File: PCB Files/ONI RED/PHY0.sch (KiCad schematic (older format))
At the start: 40 parts

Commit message: Continued routing work
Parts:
- removed C? (x2): 22pF, symbol Device:C
- removed C? (x4): 0.1uF, symbol Device:C_Small
- removed R?: 12.1k, symbol Device:R
- removed R?: 4.7K, symbol Device:R
- removed R?: 220, symbol Device:R_Small
- removed R?: 1k, symbol Device:R_Small
- removed R?: 4.7k, symbol Device:R_Small
- removed U?: KSZ9031RNXCA, Package_DFN_QFN:QFN-48-1EP_7x7mm_P0.5mm_EP5.15x5.15mm, symbol Interface_Ethernet:KSZ9031RNXCA
- removed Y?: 25MHz, symbol Device:Crystal
- added C23, C24: 22pF, symbol Device:C
- added C25, C26, C27, C28: 0.1uF, symbol Device:C_Small
- added R13: 4.7K, symbol Device:R
- added R15: 12.1k, symbol Device:R
- added R18: 1k, symbol Device:R_Small
- added R19: 220, symbol Device:R_Small
- added R7: 4.7k, symbol Device:R_Small
- added U4: KSZ9031RNXCA, Package_DFN_QFN:QFN-48-1EP_7x7mm_P0.5mm_EP5.15x5.15mm, symbol Interface_Ethernet:KSZ9031RNXCA
- added Y1: 25MHz, symbol Device:Crystal
- C10, C16: renamed from C?; value 0.1uF -> 100nF
- C11, C14, C17, C22: renamed from C?; value 0.1uF -> 10uF
- C12, C18, C21: renamed from C?; value 0.1uF -> 1uF
- gave numbers to parts that had none: 18
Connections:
- net +3.3V: now also R13.1, R19.1, R7.2, U4.1 (AVDDH), U4.12 (AVDDH), U4.16 (DVDDH), U4.34 (DVDDH), U4.40 (DVDDH)
- net AVDDL: now also U4.4 (AVDDL), U4.44 (AVDDL_PLL), U4.9 (AVDDL)
- net CLK125: now also U4.41 (CLK125_NDO/LED_MODE)
- net DVDDL: now also U4.14 (DVDDL), U4.18 (DVDDL), U4.23 (DVDDL), U4.26 (DVDDL), U4.30 (DVDDL), U4.39 (DVDDL)
- net GND: now also C23.1, C24.1, C25.2, C26.2, C27.2, C28.2, R15.2, R18.1, U4.29 (VSS), U4.49 (PAD_GND)
- net GTX_CLK: now also U4.24 (GTX_CLK)
- net INT_N: now also U4.38 (INT_N/PME_N2)
- net MDC: now also U4.36 (MDC)
- net MDIO: now also R13.2, U4.37 (MDIO)
- net M_A: now also U4.3 (TXRXM_A)
- net M_B: now also U4.6 (TXRXM_B)
- net M_C: now also U4.8 (TXRXM_C)
- net M_D: now also U4.11 (TXRXM_D)
- net PHYAD0: now also U4.17 (LED1/PHAD0/PME_N1)
- net PHYAD1: now also R18.2, U4.15 (LED2/PHYAD1)
- net PHYAD2: now also U4.35 (RX_CLK/PHYAD2)
- net P_A: now also U4.2 (TXRXP_A)
- net P_B: now also U4.5 (TXRXP_B)
- net P_C: now also U4.7 (TXRXP_C)
- net P_D: now also U4.10 (TXRXP_D)
- net RXD0: now also R7.1, U4.32 (RXD0/MODE0)
- net RXD1: now also U4.31 (RXD1/MODE1)
- net RXD2: now also U4.28 (RXD2/MODE2)
- net RX_DV: now also U4.33 (RX_DV/CLK125_EN)
- net TXD1: now also U4.20 (TXD1)
- net TXD2: now also U4.21 (TXD2)
- net TXD3: now also U4.22 (TXD3)
- net TX_EN: now also U4.25 (TX_EN)
- net at C8.1, D1.2 (A), D2.2 (A)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: now also U4.42 (RESET_N)
- net at J1.1 (MXCT3): now also C27.1
- net at J1.12 (MXCT1): now also C25.1
- net at J1.16 (LED1+): now also R19.2
- net at J1.6 (MXCT2): now also C26.1
- net at J1.7 (MXCT4): now also C28.1
- net RST renamed RESET_N
- net RX23 renamed RXD3
- net RXD3: now also U4.27 (RXD3/MODE3)
- new net: C24.2, U4.45 (XO), Y1.2
- new net: C23.2, U4.46 (XI), Y1.1
- new net: R15.1, U4.48 (ISET)
- new net TXD0: U4.19 (TXD0)

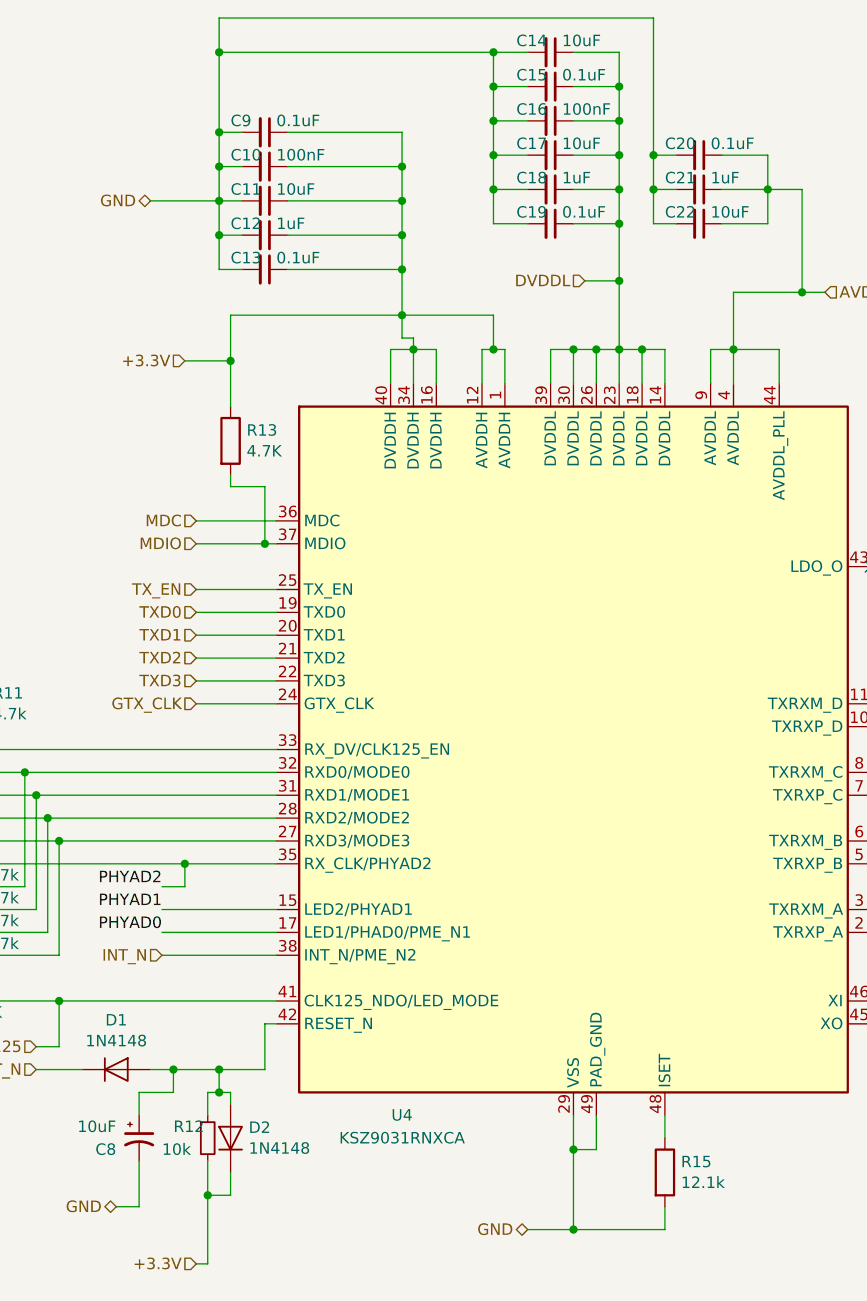
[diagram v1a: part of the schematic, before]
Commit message: Began routing PHY IO
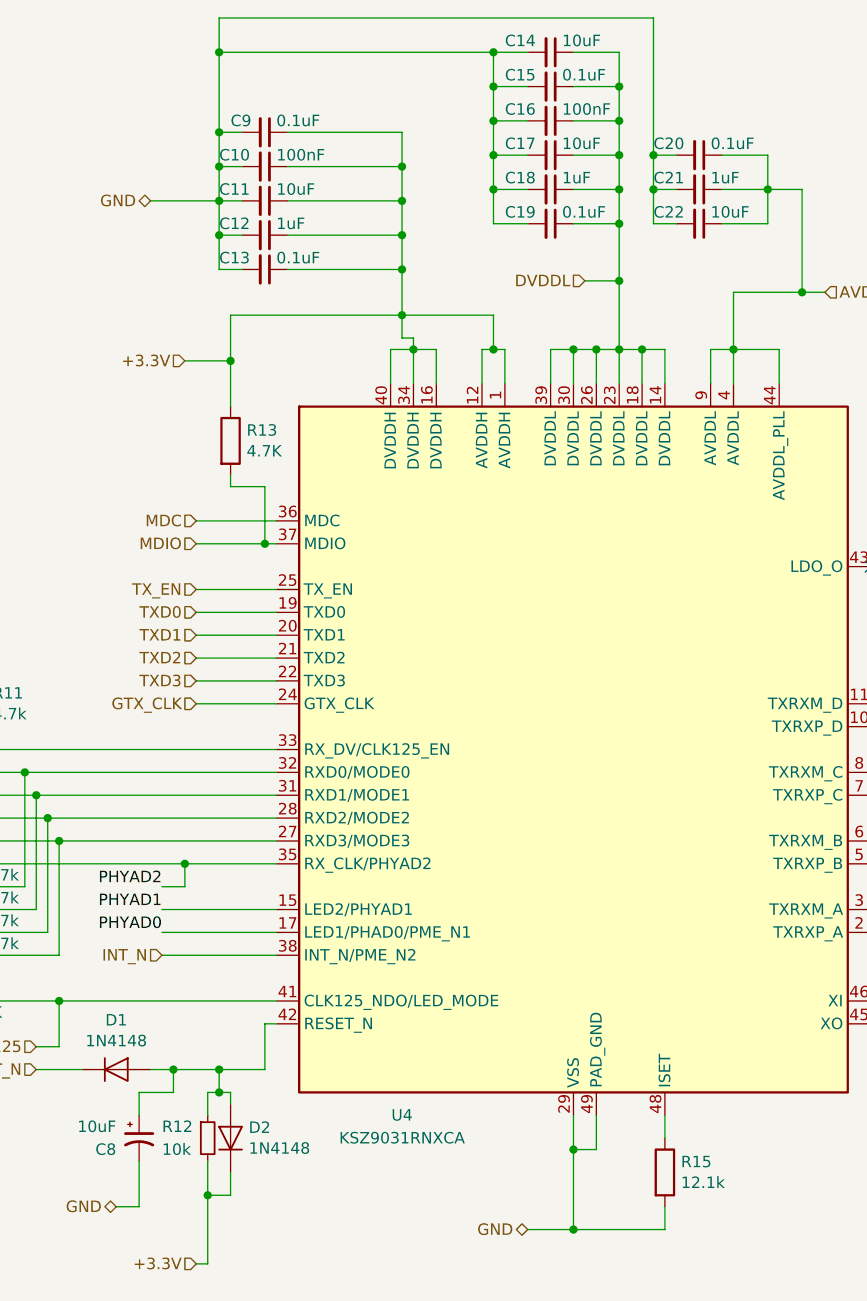
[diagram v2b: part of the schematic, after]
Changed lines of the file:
@@
 $Descr A4 11693 8268
 encoding utf-8
-Sheet 5 5
+Sheet 5 6
 Title ""
 Date ""
@@
 AR Path="/5EA74211/5ECEE10B" Ref="C13"  Part="1"
 AR Path="/5EE1B380/5ECEE10B" Ref="C?"  Part="1"
-F 0 "C13" V 2500 2100 50  0000 L CNN
+F 0 "C13" V 2500 2050 50  0000 L CNN
 F 1 "0.1uF" V 2500 2300 50  0000 L CNN
 F 2 "" H 2550 2250 50  0001 C CNN
@@
 AR Path="/5EA74211/5ECF7566" Ref="C12"  Part="1"
 AR Path="/5EE1B380/5ECF7566" Ref="C?"  Part="1"
-F 0 "C12" V 2500 1950 50  0000 L CNN
+F 0 "C12" V 2500 1900 50  0000 L CNN
 F 1 "1uF" V 2500 2150 50  0000 L CNN
 F 2 "" H 2550 2100 50  0001 C CNN
@@
 AR Path="/5EA74211/5ECF7795" Ref="C11"  Part="1"
 AR Path="/5EE1B380/5ECF7795" Ref="C?"  Part="1"
-F 0 "C11" V 2500 1800 50  0000 L CNN
+F 0 "C11" V 2500 1750 50  0000 L CNN
 F 1 "10uF" V 2500 2000 50  0000 L CNN
 F 2 "" H 2550 1950 50  0001 C CNN
@@
 AR Path="/5EA74211/5ECFD1C8" Ref="C10"  Part="1"
 AR Path="/5EE1B380/5ECFD1C8" Ref="C?"  Part="1"
-F 0 "C10" V 2500 1650 50  0000 L CNN
+F 0 "C10" V 2500 1600 50  0000 L CNN
 F 1 "100nF" V 2500 1850 50  0000 L CNN
 F 2 "" H 2550 1800 50  0001 C CNN
@@
 AR Path="/5EA74211/5ED3AA4A" Ref="C19"  Part="1"
 AR Path="/5EE1B380/5ED3AA4A" Ref="C?"  Part="1"
-F 0 "C19" V 3750 1900 50  0000 L CNN
+F 0 "C19" V 3750 1850 50  0000 L CNN
 F 1 "0.1uF" V 3750 2100 50  0000 L CNN
 F 2 "" H 3800 2050 50  0001 C CNN
@@
 AR Path="/5EA74211/5ED3AA50" Ref="C18"  Part="1"
 AR Path="/5EE1B380/5ED3AA50" Ref="C?"  Part="1"
-F 0 "C18" V 3750 1750 50  0000 L CNN
+F 0 "C18" V 3750 1700 50  0000 L CNN
 F 1 "1uF" V 3750 1950 50  0000 L CNN
 F 2 "" H 3800 1900 50  0001 C CNN
@@
 AR Path="/5EA74211/5ED3AA56" Ref="C17"  Part="1"
 AR Path="/5EE1B380/5ED3AA56" Ref="C?"  Part="1"
-F 0 "C17" V 3750 1600 50  0000 L CNN
+F 0 "C17" V 3750 1550 50  0000 L CNN
 F 1 "10uF" V 3750 1800 50  0000 L CNN
 F 2 "" H 3800 1750 50  0001 C CNN
@@
 AR Path="/5EA74211/5ED3AA5C" Ref="C16"  Part="1"
 AR Path="/5EE1B380/5ED3AA5C" Ref="C?"  Part="1"
-F 0 "C16" V 3750 1450 50  0000 L CNN
+F 0 "C16" V 3750 1400 50  0000 L CNN
 F 1 "100nF" V 3750 1650 50  0000 L CNN
 F 2 "" H 3800 1600 50  0001 C CNN
@@
 AR Path="/5EA74211/5ED3AA62" Ref="C15"  Part="1"
 AR Path="/5EE1B380/5ED3AA62" Ref="C?"  Part="1"
-F 0 "C15" V 3750 1300 50  0000 L CNN
+F 0 "C15" V 3750 1250 50  0000 L CNN
 F 1 "0.1uF" V 3750 1500 50  0000 L CNN
 F 2 "" H 3800 1450 50  0001 C CNN
@@
 AR Path="/5EA74211/5ED41050" Ref="C14"  Part="1"
 AR Path="/5EE1B380/5ED41050" Ref="C?"  Part="1"
-F 0 "C14" V 3750 1150 50  0000 L CNN
+F 0 "C14" V 3750 1100 50  0000 L CNN
 F 1 "10uF" V 3750 1350 50  0000 L CNN
 F 2 "" H 3800 1300 50  0001 C CNN
@@
 AR Path="/5EA74211/5EDA88AB" Ref="C22"  Part="1"
 AR Path="/5EE1B380/5EDA88AB" Ref="C?"  Part="1"
-F 0 "C22" V 4400 1900 50  0000 L CNN
+F 0 "C22" V 4400 1850 50  0000 L CNN
 F 1 "10uF" V 4400 2100 50  0000 L CNN
 F 2 "" H 4450 2050 50  0001 C CNN
@@
 AR Path="/5EA74211/5EDA8B26" Ref="C21"  Part="1"
 AR Path="/5EE1B380/5EDA8B26" Ref="C?"  Part="1"
-F 0 "C21" V 4400 1750 50  0000 L CNN
+F 0 "C21" V 4400 1700 50  0000 L CNN
 F 1 "1uF" V 4400 1950 50  0000 L CNN
 F 2 "" H 4450 1900 50  0001 C CNN
@@
 AR Path="/5EA74211/5EDA8C47" Ref="C20"  Part="1"
 AR Path="/5EE1B380/5EDA8C47" Ref="C?"  Part="1"
-F 0 "C20" V 4400 1600 50  0000 L CNN
+F 0 "C20" V 4400 1550 50  0000 L CNN
 F 1 "0.1uF" V 4400 1800 50  0000 L CNN
 F 2 "" H 4450 1750 50  0001 C CNN
@@
 AR Path="/5EA74211/5EF2ABEF" Ref="R12"  Part="1"
 AR Path="/5EE1B380/5EF2ABEF" Ref="R?"  Part="1"
-F 0 "R12" H 2150 6100 50  0000 L CNN
+F 0 "R12" H 2100 6100 50  0000 L CNN
 F 1 "10k" H 2100 6000 50  0000 L CNN
 F 2 "" H 2300 6050 50  0001 C CNN
@@
 Wire Wire Line
 	1650 5650 1650 5450
-Wire Bus Line
-	7350 3500 7350 5000
-Wire Bus Line
-	5700 3500 5700 5100
 Connection ~ 1650 5450
 Wire Wire Line
@@
 Text HLabel 850  4850 0    50   Input ~ 0
 RX_CLK
+Wire Bus Line
+	7350 3500 7350 5000
+Wire Bus Line
+	5700 3500 5700 5100
 $EndSCHEMATC
